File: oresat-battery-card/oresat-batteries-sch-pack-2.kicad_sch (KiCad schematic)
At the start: 92 parts, among them Q11 SI7111EDN-T1-GE3, Q22 SQS484ENW-T1_GE3, Q24 DMN2053UQ-13, Q25 DMN2053UQ-13, Q26 DMN2053UQ-13, Q27 DMN2053UQ-13, Q31 SI7111EDN-T1-GE3, Q32 DMP2035UQ-7, Q33 DMP2035UQ-7, Q34 SI7111EDN-T1-GE3, Q35 SI7111EDN-T1-GE3, Q36 SI7111EDN-T1-GE3, Q37 SI7111EDN-T1-GE3, Q40 DMP2035UQ-7, U13 S-8209AAA-T8T1U, U14 S-8209AAA-T8T1U, U15 TPS25983, U16 LTC4412, U17 MAX17205G

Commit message: Jumped back on the TPS bandwagon - LCSC to the rescue! - and lots of cleanup.
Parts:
- removed Q11: SI7111EDN-T1-GE3, Package_SO:Vishay_PowerPAK_1212-8_Single, symbol Transistor_FET:SiS443DN
- removed R70: 100k, oresat-passives:0603-C-NOSILK, symbol Device:R_Small_US
- JP3, JP4: now not fitted
- R75, R78, R82, R83: DPN RMCF0603FT2K70CT-ND -> RMCF0603FT1K00CT-ND
- U15: value TPS25983 -> TPS259830ONRGER; DPN 296-TPS259830LNRGERCT-ND -> 296-TPS259830ONRGERCT-ND; MPN TPS25983 -> TPS259830ONRGER
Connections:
- net POS-BATT-DISC: now also R116.1, R117.2, U15.6 (EN/UVLO)
- net VBUS: now also C11.1, C34.1, Q31.1 (S), Q31.2 (S), Q31.3 (S), Q36.5 (D), TP59.1, U16.1 (VIN)
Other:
- note added: "Q22 disconnects the - battery lead, but it also kills the ground reference for the ~{SHUTDOOWN} circuit, which is bad because it turns on the ABLIC and MAX17 chips. So, R94 preserves the ground reference while not allowing any appreciable current to flow."
- note removed: "Q22 disconnects the - battery lead, but it also kills the ground reference for the ~{SHUTDOOWN} circuit, which is bad because it turns on the ABLIC and MAX17 chips. So, R94 preserves the ground reference while not allow anny appreciable current to flow."
- moved on the sheet: B3, B4, C11, C26, C27, C28, C29, C30, C31, C32, C33, C34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

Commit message: Battery Card 4.0, no ERC or DRC errors or warnings
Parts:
- added TP60: TEST-POINT-LARGE-SQUARE, oresat-misc:TestPoint-0.75mm-th, symbol oresat-misc:Test-Point-0.75mm-th
- R110: value 210 -> 154; DPN RMCF0603FT100KCT-ND -> 738-RMCF0603FT154RCT-ND; MPN RMCF0603FT100K -> RMCF0603FT154R
- R112: value 210 -> 1k; DPN RMCF0603FT100KCT-ND -> RMCF0603FT1K00CT-ND; MPN RMCF0603FT100K -> RMCF0603FT1K00
- R116: value 100k -> 357k; DPN RMCF0603FT100KCT-ND -> RMCF0603FT357KCT-ND; MPN RMCF0603FT100K -> RMCF0603FT357K
- R56: value 100k -> 2; DPN RMCF0603FT100KCT-ND -> RMCF0603FT2R00DKR-ND; MPN RMCF0603FT100K -> RMCF0603FT2R00
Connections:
- net at R112.1, U15.9 (IMON): now also TP60.1
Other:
- note added: "EFUSE Current limit: 8.0 A (circuit breaker set to +20%, 9.6 A) Voltage ramp up time: 24 ms Transient overcurrent timer: 2.0 ms Time between retries: 4.6 s"
- note added: "TVS diode is next to main connector"
- note removed: "EFUSE Current limit: 7.1 A Voltage ramp up time: 24 ms Transient overcurrent timer: 2.0 ms Time between retries: 4.6 s"
- moved on the sheet: B3, B4, C11, C26, C27, C28, C29, C30, C31, C32, C33, C34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

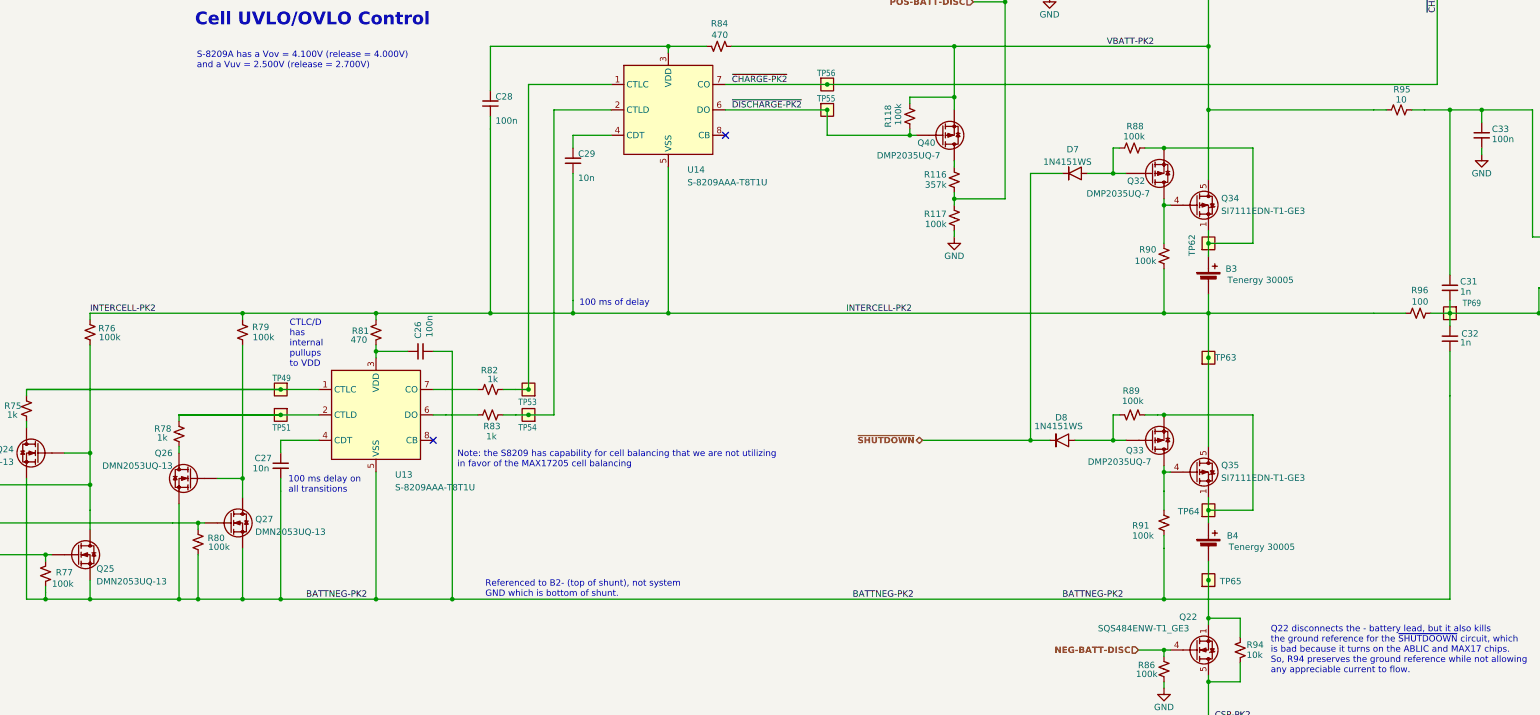
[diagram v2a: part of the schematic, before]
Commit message: Updated Makefile and Readme; fixed TCAN IC, cleanup, fix battery connections that were killed somehow
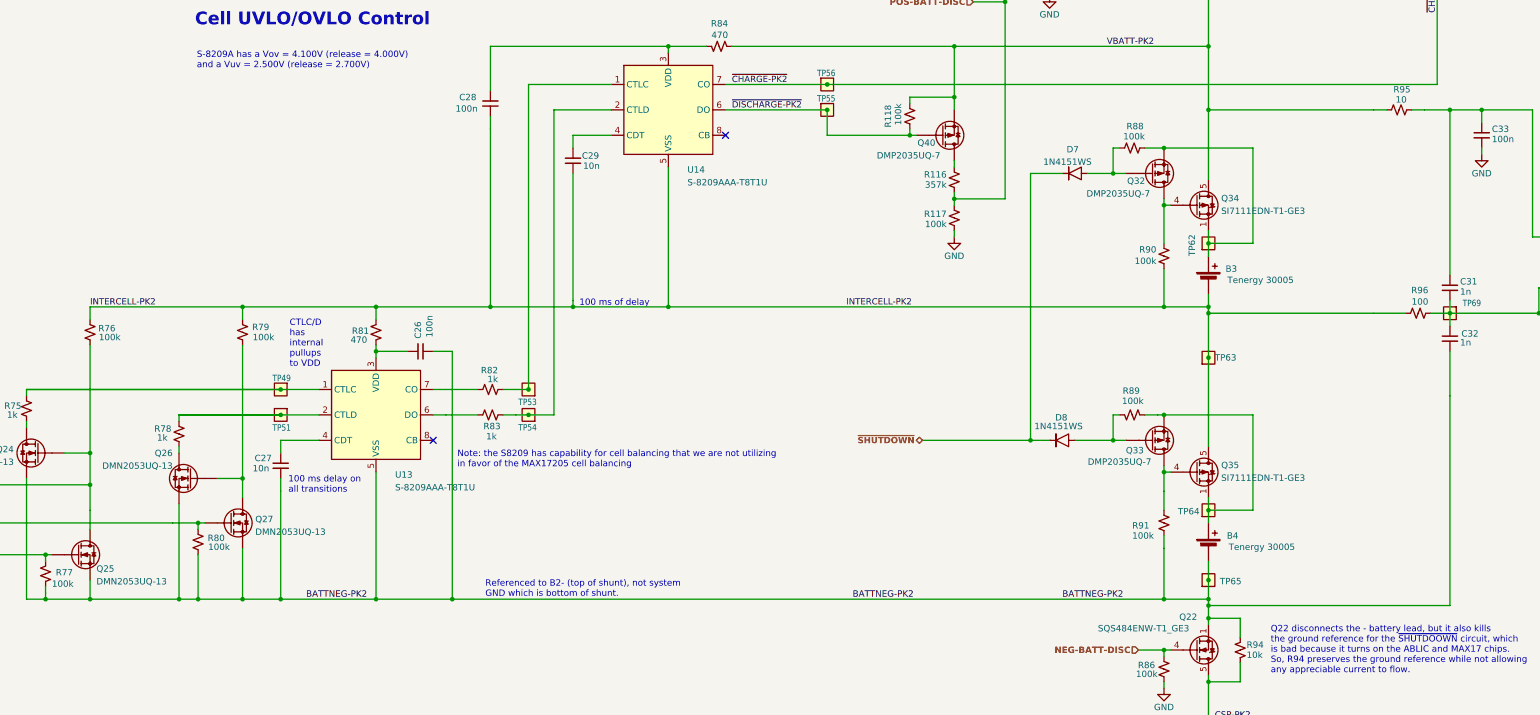
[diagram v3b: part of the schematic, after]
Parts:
- C62: DPN 399-6856-1-ND -> 399-12984-1-ND; MPN C0603C104K5RACAUTO -> C0603C153K5RACAUTO
- R56: DPN RMCF0603FT2R00DKR-ND -> RMCF0603FT2R00CT-ND
- R92: DPN 696-1374-1-ND -> WSLP-.01CT-ND; MFR Riedon -> Vishay Dale; MPN CSR1206-0R01F1 -> WSLP1206R0100FEA
- U16: DPN MAX4211FETE+-ND -> LTC4412ES6#WTRMPBF; MPN MAX4211FETE -> LTC4412ES6#PBF
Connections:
- net BATTNEG-PK2: now also B4.2 (-), Q22.1 (S), Q22.2 (S), Q22.3 (S), R94.2, TP65.1

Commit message: Changes to eFuse after trying evaluation board, and recalculating values, and trying to reduce number of passive components to minimum number
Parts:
- C27, C29: value 10n -> 15n; DPN 399-12983-1-ND -> 399-12984-1-ND; MPN C0603C103J5RACAUTO -> C0603C153K5RACAUTO
- C61: value 100n -> 15n; DPN 399-6856-1-ND -> 399-12984-1-ND; MPN C0603C104K5RACAUTO -> C0603C153K5RACAUTO
- R112: value 1k -> 470; DPN RMCF0603FT1K00CT-ND -> RMCF0603FT470RCT-ND; MPN RMCF0603FT1K00 -> RMCF0603FT470R
- R116: value 357k -> 330k; DPN RMCF0603FT357KCT-ND -> RMCF0603FT330KCT-ND; MPN RMCF0603FT357K -> RMCF0603FT330K
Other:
- note added: "150 ms delay on all transitions"
- note added: "EFUSE Current limit: 8.0 A (set +20% to Rilim = 154 ohm = 9.6 A) Transient overcurrent timer: 15 n = 5 ms Fast current limit = 210% * 9.6 A = 20.16 A Voltage ramp up time: 24 ms Time between retries: 4.6 s"
- note added: "Vbatt = 6.0V -> EN/UVL = 1.39 V which is above 1.23 V cutoff"
- note removed: "100 ms delay on all transitions"
- note removed: "100 ms of delay"
- note removed: "EFUSE Current limit: 8.0 A (circuit breaker set to +20%, 9.6 A) Voltage ramp up time: 24 ms Transient overcurrent timer: 2.0 ms Time between retries: 4.6 s"
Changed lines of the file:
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@@
 		)
 	)
+	(text "150 ms delay on\nall transitions"
+		(exclude_from_sim no)
+		(at 249.428 214.122 0)
+		(effects
+			(font
+				(size 1.27 1.27)
+			)
+			(justify left bottom)
+		)
+	)
 	(text "1206"
 		(exclude_from_sim no)
@@
 		)
 	)
+	(text "EFUSE\n\nCurrent limit: 8.0 A (set +20% to Rilim = 154 ohm = 9.6 A)\nTransient overcurrent timer: 15 n = 5 ms\nFast current limit = 210% * 9.6 A = 20.16 A\n\nVoltage ramp up time: 24 ms\nTime between retries: 4.6 s"
+		(exclude_from_sim no)
+		(at 250.19 150.622 0)
+		(effects
+			(font
+				(size 1.27 1.27)
+			)
+		)
+	)
 	(text "Off board on leads, thermally\nconnected to battery cells"
 		(exclude_from_sim no)
@@
 		)
 	)
-	(text "DISCHARGE ONLY IF:\n1) Vcell > Voverdisch\n2) DISCHARGE_DISABLE is not asserted."
+	(text "Vbatt = 6.0V -> EN/UVL = 1.39 V\nwhich is above 1.23 V cutoff"
 		(exclude_from_sim no)
-		(at 237.236 146.05 0)
+		(at 304.292 223.774 0)
 		(effects
 			(font
 				(size 1.27 1.27)
 			)
-			(justify left bottom)
 		)
 	)
-	(text "Note: the S8209 has capability for cell balancing that we are not utilizing\nin favor of the MAX17205 cell balancing"
+	(text "DISCHARGE ONLY IF:\n1) Vcell > Voverdisch\n2) DISCHARGE_DISABLE is not asserted."
 		(exclude_from_sim no)
-		(at 224.536 268.478 0)
+		(at 263.906 105.664 0)
 		(effects
 			(font
@@
 		)
 	)
-	(text "B1"
+	(text "Note: the S8209 has capability for cell balancing that we are not utilizing\nin favor of the MAX17205 cell balancing"
 		(exclude_from_sim no)
-		(at 484.124 271.78 0)
+		(at 224.536 268.478 0)
 		(effects
 			(font
@@
 		)
 	)
-	(text "100 ms of delay"
+	(text "B1"
 		(exclude_from_sim no)
-		(at 248.92 236.22 0)
+		(at 484.124 271.78 0)
 		(effects
 			(font
@@
 	(text "(Current flows when Vbat > Vbus)"
 		(exclude_from_sim no)
-		(at 279.146 103.632 0)
+		(at 272.542 97.028 0)
 		(effects
 			(font
@@
 		)
 	)
-	(text "EFUSE\n\nCurrent limit: 8.0 A (circuit breaker set to +20%, 9.6 A)\nVoltage ramp up time: 24 ms\nTransient overcurrent timer: 2.0 ms\nTime between retries: 4.6 s"
-		(exclude_from_sim no)
-		(at 248.666 131.318 0)
-		(effects
-			(font
-				(size 1.27 1.27)
-			)
-		)
-	)
 	(text "Discharge Control"
 		(exclude_from_sim no)
@@
 		)
 	)
-	(text "100 ms delay on\nall transitions"
+	(text "150 ms delay on\nall transitions"
 		(exclude_from_sim no)
 		(at 190.754 273.558 0)
@@
 			)
 		)
-		(property "Value" "100n"
+		(property "Value" "15n"
 			(at 297.688 139.7 0)
 			(show_name no)
@@
 			)
 		)
-		(property "Datasheet" "https://search.kemet.com/download/specsheet/C0603C104K5RACAUTO"
+		(property "Datasheet" "https://yageogroup.com/content/datasheet/asset/file/KEM_C1023_X7R_AUTO_SMD"
 			(at 295.91 138.43 0)
 			(hide yes)
@@
 			)
 		)
-		(property "Description" "0.1 µF ±10% 50V Ceramic Capacitor X7R 0603 (1608 Metric)"
+		(property "Description" "0.015 µF ±10% 50V Ceramic Capacitor X7R 0603 (1608 Metric)"
 			(at 295.91 138.43 0)
 			(hide yes)
@@
 			)
 		)
-		(property "DPN" "399-6856-1-ND"
+		(property "DPN" "399-12984-1-ND"
 			(at 295.91 138.43 0)
 			(hide yes)
@@
 			)
 		)
-		(property "MPN" "C0603C104K5RACAUTO"
+		(property "MPN" "C0603C153K5RACAUTO"
 			(at 295.91 138.43 0)
 			(hide yes)
@@
 			)
 		)
-		(property "Value" "10n"
+		(property "Value" "15n"
 			(at 249.682 208.788 0)
 			(show_name no)
@@
 			)
 		)
-		(property "Datasheet" "https://www.yageogroup.com/content/datasheet/asset/file/KEM_C1023_X7R_AUTO_SMD"
+		(property "Datasheet" "https://yageogroup.com/content/datasheet/asset/file/KEM_C1023_X7R_AUTO_SMD"
 			(at 247.65 207.01 0)
 			(hide yes)
@@
 			)
 		)
-		(property "Description" "10000 pF ±5% 50V Ceramic Capacitor X7R 0603 (1608 Metric)"
+		(property "Description" "0.015 µF ±10% 50V Ceramic Capacitor X7R 0603 (1608 Metric)"
 			(at 247.65 207.01 0)
 			(hide yes)
@@
 			)
 		)
-		(property "DPN" "399-12983-1-ND"
+		(property "DPN" "399-12984-1-ND"
 			(at 247.65 207.01 0)
 			(hide yes)
@@
 			)
 		)
-		(property "MPN" "C0603C103J5RACAUTO"
+		(property "MPN" "C0603C153K5RACAUTO"
 			(at 247.65 207.01 0)
 			(hide yes)
@@
 			)
 		)
-		(property "Value" "10n"
+		(property "Value" "15n"
 			(at 186.944 269.24 0)
 			(show_name no)
@@
 			)
 		)
-		(property "Datasheet" "https://www.yageogroup.com/content/datasheet/asset/file/KEM_C1023_X7R_AUTO_SMD"
+		(property "Datasheet" "https://yageogroup.com/content/datasheet/asset/file/KEM_C1023_X7R_AUTO_SMD"
 			(at 189.23 267.97 0)
 			(hide yes)
@@
 			)
 		)
-		(property "Description" "10000 pF ±5% 50V Ceramic Capacitor X7R 0603 (1608 Metric)"
+		(property "Description" "0.015 µF ±10% 50V Ceramic Capacitor X7R 0603 (1608 Metric)"
 			(at 189.23 267.97 0)
 			(hide yes)
@@
 			)
 		)
-		(property "DPN" "399-12983-1-ND"
+		(property "DPN" "399-12984-1-ND"
 			(at 189.23 267.97 0)
 			(hide yes)
@@
 			)
 		)
-		(property "MPN" "C0603C103J5RACAUTO"
+		(property "MPN" "C0603C153K5RACAUTO"
 			(at 189.23 267.97 0)
 			(hide yes)
@@
 			)
 		)
-		(property "Value" "1k"
+		(property "Value" "470"
 			(at 281.686 140.208 0)
 			(show_name no)
@@
 			)
 		)
-		(property "Description" "1 kOhms ±1% 0.1W, 1/10W Chip Resistor 0603 (1608 Metric) Automotive AEC-Q200 Thick Film"
+		(property "Description" "470 Ohms ±1% 0.1W, 1/10W Chip Resistor 0603 (1608 Metric) Automotive AEC-Q200 Thick Film"
 			(at 283.21 138.43 0)
 			(hide yes)
@@
 			)
 		)
-		(property "DPN" "RMCF0603FT1K00CT-ND"
+		(property "DPN" "RMCF0603FT470RCT-ND"
 			(at 283.21 138.43 0)
 			(hide yes)
@@
 			)
 		)
-		(property "MPN" "RMCF0603FT1K00"
+		(property "MPN" "RMCF0603FT470R"
 			(at 283.21 138.43 0)
 			(hide yes)
@@
 			)
 		)
-		(property "Value" "357k"
+		(property "Value" "330k"
 			(at 322.326 211.074 0)
 			(show_name no)
@@
 			)
 		)
-		(property "Description" "357 kOhms ±1% 0.1W, 1/10W Chip Resistor 0603 (1608 Metric) Automotive AEC-Q200 Thick Film"
+		(property "Description" "330 kOhms ±1% 0.1W, 1/10W Chip Resistor 0603 (1608 Metric) Automotive AEC-Q200 Thick Film"
 			(at 323.85 210.82 0)
 			(hide yes)
@@
 			)
 		)
-		(property "DPN" "RMCF0603FT357KCT-ND"
+		(property "DPN" "RMCF0603FT330KCT-ND"
 			(at 323.85 210.82 0)
 			(hide yes)
@@
 			)
 		)
-		(property "MPN" "RMCF0603FT357K"
+		(property "MPN" "RMCF0603FT330K"
 			(at 323.85 210.82 0)
 			(hide yes)

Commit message: Added imon capabilities, cleaned up some lingering DRCs that kept popping back up.
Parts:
- added C68: 100n, oresat-passives:0603-C-NOSILK, symbol Device:C_Small
- added R121: 10k, oresat-passives:0603-C-NOSILK, symbol Device:R_Small_US
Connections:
- net GND: now also C68.2
- net at R112.1, TP60.1, U15.9 (IMON): now also R121.1
- new net IMON-PK2: C68.1, R121.2

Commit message: Changes after inventory check and BOM check
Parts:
- C35, C36: DPN 399-6820-1-ND -> 399-C0603C474K3RACAUTOCT-ND; MPN C0603C473K5RACAUTO -> C0603C474K3RACAUTO
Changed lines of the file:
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@@
 			)
 		)
-		(property "Datasheet" "https://search.kemet.com/download/specsheet/C0603C473K5RACAUTO"
-			(at 485.14 198.12 0)
-			(hide yes)
-			(show_name no)
-			(do_not_autoplace no)
-			(effects
-				(font
-					(size 1.27 1.27)
-				)
-			)
-		)
-		(property "Description" "0.047 µF ±10% 50V Ceramic Capacitor X7R 0603 (1608 Metric)"
+		(property "Datasheet" "https://www.yageogroup.com/content/datasheet/asset/file/KEM_C1023_X7R_AUTO_SMD"
+			(at 485.14 198.12 0)
+			(hide yes)
+			(show_name no)
+			(do_not_autoplace no)
+			(effects
+				(font
+					(size 1.27 1.27)
+				)
+			)
+		)
+		(property "Description" "0.47 µF ±10% 25V Ceramic Capacitor X7R 0603 (1608 Metric)"
 			(at 485.14 198.12 0)
 			(hide yes)
@@
 			)
 		)
-		(property "DPN" "399-6820-1-ND"
+		(property "DPN" "399-C0603C474K3RACAUTOCT-ND"
 			(at 485.14 198.12 0)
 			(hide yes)
@@
 			)
 		)
-		(property "MPN" "C0603C473K5RACAUTO"
+		(property "MPN" "C0603C474K3RACAUTO"
 			(at 485.14 198.12 0)
 			(hide yes)
@@
 			)
 		)
-		(property "Datasheet" "https://search.kemet.com/download/specsheet/C0603C473K5RACAUTO"
-			(at 474.98 198.12 0)
-			(hide yes)
-			(show_name no)
-			(do_not_autoplace no)
-			(effects
-				(font
-					(size 1.27 1.27)
-				)
-			)
-		)
-		(property "Description" "0.047 µF ±10% 50V Ceramic Capacitor X7R 0603 (1608 Metric)"
+		(property "Datasheet" "https://www.yageogroup.com/content/datasheet/asset/file/KEM_C1023_X7R_AUTO_SMD"
+			(at 474.98 198.12 0)
+			(hide yes)
+			(show_name no)
+			(do_not_autoplace no)
+			(effects
+				(font
+					(size 1.27 1.27)
+				)
+			)
+		)
+		(property "Description" "0.47 µF ±10% 25V Ceramic Capacitor X7R 0603 (1608 Metric)"
 			(at 474.98 198.12 0)
 			(hide yes)
@@
 			)
 		)
-		(property "DPN" "399-6820-1-ND"
+		(property "DPN" "399-C0603C474K3RACAUTOCT-ND"
 			(at 474.98 198.12 0)
 			(hide yes)
@@
 			)
 		)
-		(property "MPN" "C0603C473K5RACAUTO"
-			(at 474.98 198.12 0)
-			(hide yes)
+		(property "MPN" "C0603C474K3RACAUTO"
+			(at 474.98 198.12 0)
+			(hide yes)
